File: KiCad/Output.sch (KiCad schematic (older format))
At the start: 19 parts, among them J3 Conn_01x08, U43 74LS574

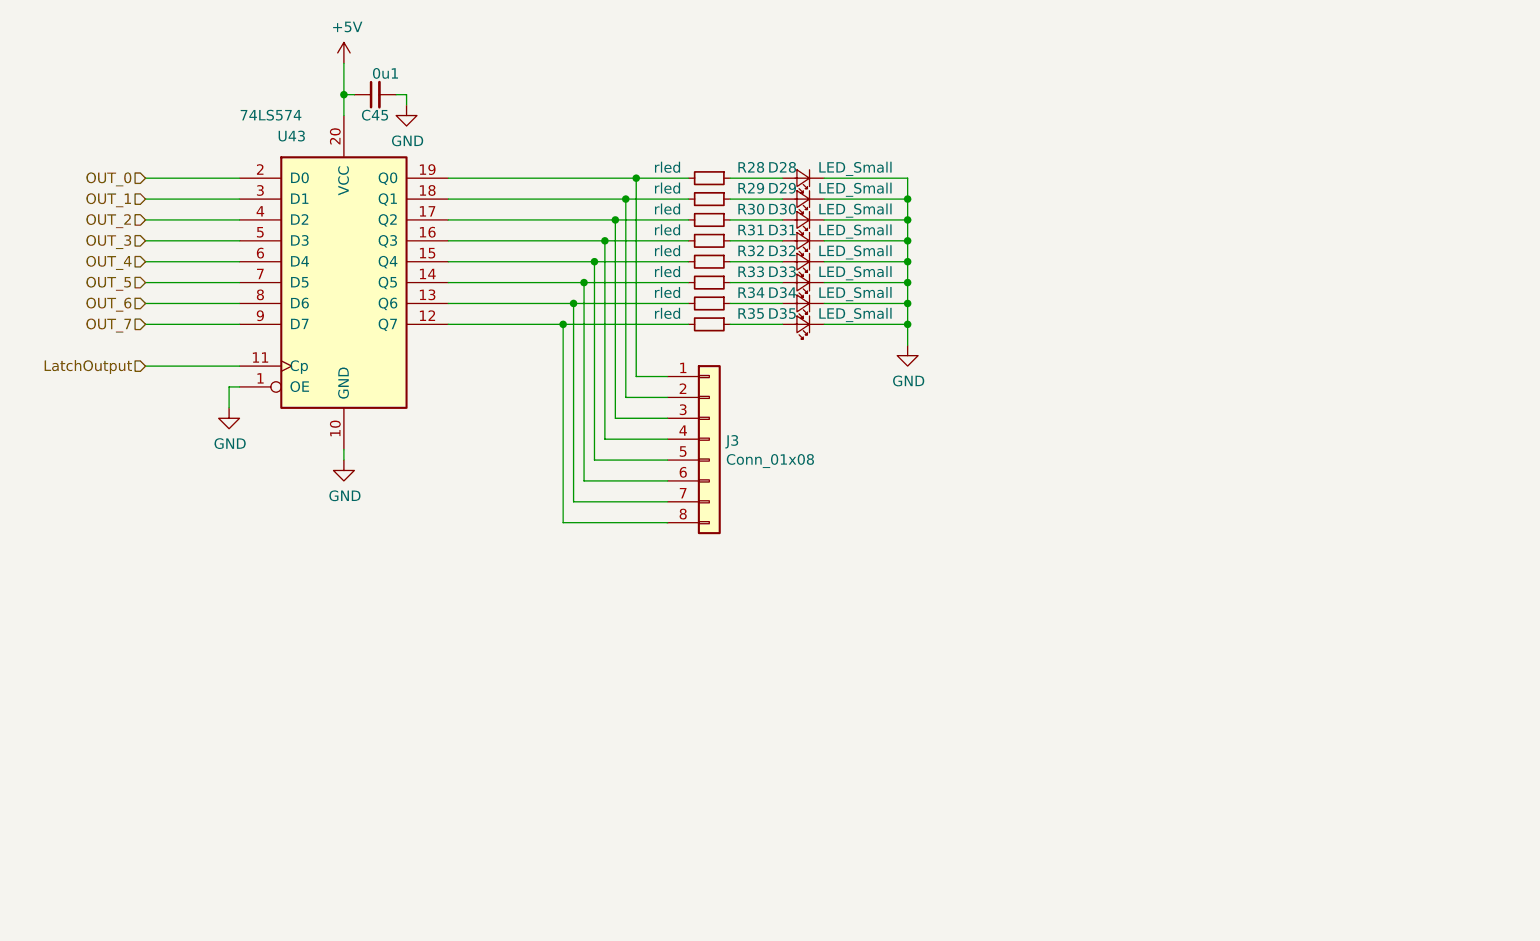
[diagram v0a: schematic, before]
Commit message: Schematic Update First Draft, ERC Passed
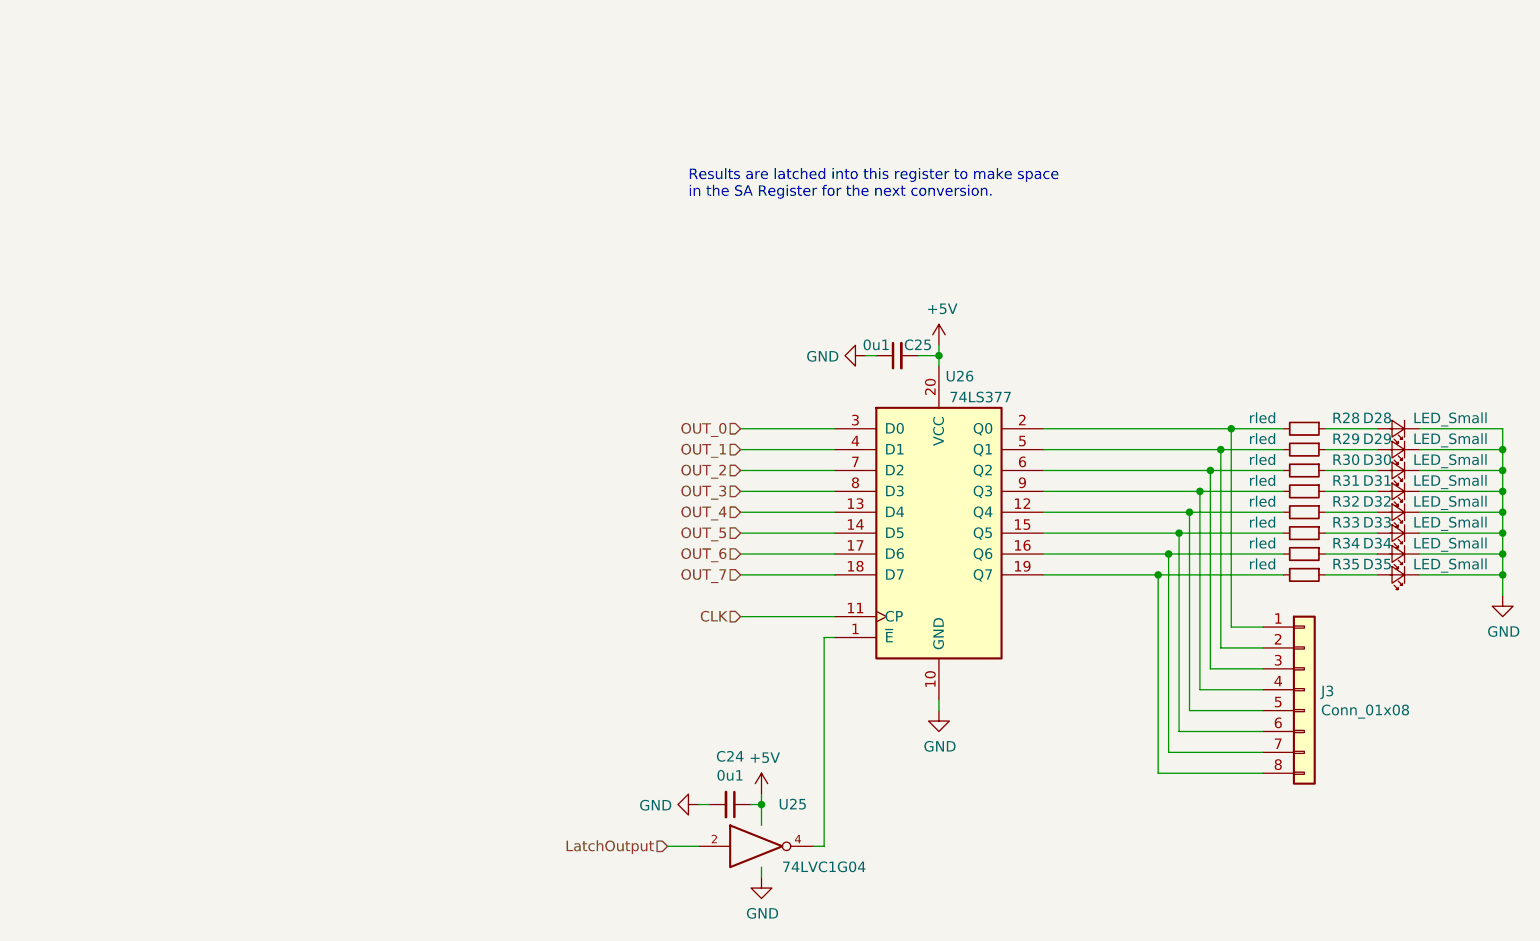
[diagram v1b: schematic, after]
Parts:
- removed C45: 0u1, Capacitor_SMD:C_0603_1608Metric, symbol Device:C_Small
- removed U43: 74LS574, Package_SO:SOIC-20W_7.5x12.8mm_P1.27mm, symbol 74xx:74LS574
- added C24, C25: 0u1, Capacitor_SMD:C_0603_1608Metric, symbol Device:C_Small
- added U25: 74LVC1G04, Package_TO_SOT_SMD:SOT-353_SC-70-5, symbol 74xGxx:74LVC1G04
- added U26: 74LS377, Package_SO:SOIC-20W_7.5x12.8mm_P1.27mm, symbol 74xx:74LS377
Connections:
- net +5V: now also C24.1, C25.2, U25.5 (VCC), U26.20 (VCC)
- net GND: now also C24.2, C25.1, U25.3 (GND), U26.10 (GND)
- net LatchOutput: now also U25.2
- net OUT_0: now also U26.3 (D0)
- net OUT_1: now also U26.4 (D1)
- net OUT_2: now also U26.7 (D2)
- net OUT_3: now also U26.8 (D3)
- net OUT_4: now also U26.13 (D4)
- net OUT_5: now also U26.14 (D5)
- net OUT_6: now also U26.17 (D6)
- net OUT_7: now also U26.18 (D7)
- net at J3.1 (Pin_1), R28.2: now also U26.2 (Q0)
- net at J3.2 (Pin_2), R29.2: now also U26.5 (Q1)
- net at J3.3 (Pin_3), R30.2: now also U26.6 (Q2)
- net at J3.4 (Pin_4), R31.2: now also U26.9 (Q3)
- net at J3.5 (Pin_5), R32.2: now also U26.12 (Q4)
- net at J3.6 (Pin_6), R33.2: now also U26.15 (Q5)
- net at J3.7 (Pin_7), R34.2: now also U26.16 (Q6)
- net at J3.8 (Pin_8), R35.2: now also U26.19 (Q7)
- new net: U25.4, U26.1 (~E)
- new net CLK: U26.11 (CP)
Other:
- note added: "Results are latched into this register to make space\nin the SA Register for the next conversion."
- moved on the sheet: D28, D29, D30, D31, D32, D33, D34, D35, J3, R28, R29, R30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

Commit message: First part placement
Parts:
- D28, D29, D30, D31, D32, D33, D34, D35: footprint LED_SMD:LED_0805_2012Metric -> LED_SMD:LED_0603_1608Metric
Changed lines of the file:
@@
 F 0 "D28" H 7500 2700 50  0000 C CNN
 F 1 "LED_Small" H 7150 2700 50  0000 C CNN
-F 2 "LED_SMD:LED_0805_2012Metric" V 7400 2750 50  0001 C CNN
+F 2 "LED_SMD:LED_0603_1608Metric" V 7400 2750 50  0001 C CNN
 F 3 "~" V 7400 2750 50  0001 C CNN
 	1    7400 2750
@@
 F 0 "D35" H 7500 3400 50  0000 C CNN
 F 1 "LED_Small" H 7150 3400 50  0000 C CNN
-F 2 "LED_SMD:LED_0805_2012Metric" V 7400 3450 50  0001 C CNN
+F 2 "LED_SMD:LED_0603_1608Metric" V 7400 3450 50  0001 C CNN
 F 3 "~" V 7400 3450 50  0001 C CNN
 	1    7400 3450
@@
 F 0 "D34" H 7500 3300 50  0000 C CNN
 F 1 "LED_Small" H 7150 3300 50  0000 C CNN
-F 2 "LED_SMD:LED_0805_2012Metric" V 7400 3350 50  0001 C CNN
+F 2 "LED_SMD:LED_0603_1608Metric" V 7400 3350 50  0001 C CNN
 F 3 "~" V 7400 3350 50  0001 C CNN
 	1    7400 3350
@@
 F 0 "D33" H 7500 3200 50  0000 C CNN
 F 1 "LED_Small" H 7150 3200 50  0000 C CNN
-F 2 "LED_SMD:LED_0805_2012Metric" V 7400 3250 50  0001 C CNN
+F 2 "LED_SMD:LED_0603_1608Metric" V 7400 3250 50  0001 C CNN
 F 3 "~" V 7400 3250 50  0001 C CNN
 	1    7400 3250
@@
 F 0 "D32" H 7500 3100 50  0000 C CNN
 F 1 "LED_Small" H 7150 3100 50  0000 C CNN
-F 2 "LED_SMD:LED_0805_2012Metric" V 7400 3150 50  0001 C CNN
+F 2 "LED_SMD:LED_0603_1608Metric" V 7400 3150 50  0001 C CNN
 F 3 "~" V 7400 3150 50  0001 C CNN
 	1    7400 3150
@@
 F 0 "D31" H 7500 3000 50  0000 C CNN
 F 1 "LED_Small" H 7150 3000 50  0000 C CNN
-F 2 "LED_SMD:LED_0805_2012Metric" V 7400 3050 50  0001 C CNN
+F 2 "LED_SMD:LED_0603_1608Metric" V 7400 3050 50  0001 C CNN
 F 3 "~" V 7400 3050 50  0001 C CNN
 	1    7400 3050
@@
 F 0 "D30" H 7500 2900 50  0000 C CNN
 F 1 "LED_Small" H 7150 2900 50  0000 C CNN
-F 2 "LED_SMD:LED_0805_2012Metric" V 7400 2950 50  0001 C CNN
+F 2 "LED_SMD:LED_0603_1608Metric" V 7400 2950 50  0001 C CNN
 F 3 "~" V 7400 2950 50  0001 C CNN
 	1    7400 2950
@@
 F 0 "D29" H 7500 2800 50  0000 C CNN
 F 1 "LED_Small" H 7150 2800 50  0000 C CNN
-F 2 "LED_SMD:LED_0805_2012Metric" V 7400 2850 50  0001 C CNN
+F 2 "LED_SMD:LED_0603_1608Metric" V 7400 2850 50  0001 C CNN
 F 3 "~" V 7400 2850 50  0001 C CNN
 	1    7400 2850
